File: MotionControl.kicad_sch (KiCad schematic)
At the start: 25 parts, among them J2 Conn_ARM_JTAG_SWD_10, Q1 2N7002, SW1 SW_Push, U1 ATSAMD21J18A-A, U7 TC4427, Y1 32.768kHz

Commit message: begin work on optical inputs, finish mag sensors
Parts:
- added J15: Conn_01x05_Pin, Connector_PinSocket_2.00mm:PinSocket_1x05_P2.00mm_Vertical, symbol Connector:Conn_01x05_Socket
- R8, R9: value 130R -> 165R; Part RC0402FR-07130RL -> RC0402FR-07165RL
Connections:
- net GND: now also J15.1 (Pin_1)
- net Mag Sensors/PWM1: now also J15.2 (Pin_2)
- net Mag Sensors/PWM2: now also J15.3 (Pin_3)
- net Mag Sensors/PWM3: now also J15.4 (Pin_4)
- net Mag Sensors/PWM4: now also J15.5 (Pin_5)
- net PB10_MAG_MOSI: now reaches U1.23 (PB10)
- net PB11_MAG_SCK: now reaches U1.24 (PB11)
- net PB12_MAG_CSn3: now reaches U1.25 (PB12)
- net PB13_MAG_CSn2: now reaches U1.26 (PB13)
- net PA18_MAG_CSn4: now reaches U1.37 (PA18)
- net PA22_MAG_MISO: now reaches U1.43 (PA22)
- net PA23_MAG_CSn1: now reaches U1.44 (PA23)
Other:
- added sheet Optical Sensors (opticalins.kicad_sch)

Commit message: cs routing changes, endstop stuff
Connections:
- net PA18_MAG_CSn4: now also U1.27 (PB14); no longer U1.37 (PA18)
- net PB07_ES5: now reaches U1.10 (PB07)
- net PB08_ES6: now reaches U1.11 (PB08)
- net PB06_ES7: now reaches U1.12 (PB09)
- net PB15_ES8: now reaches U1.28 (PB15)
- net PB16_ES9: now reaches U1.39 (PB16)
- net PB17_ES10: now reaches U1.40 (PB17)
- net PB22_ES11: now reaches U1.49 (PB22)
- net PB23_ES12: now reaches U1.50 (PB23)
- net PB30_MAG_CSn1: now reaches U1.59 (PB30)
- net PB05_ES3: now reaches U1.6 (PB05)
- net PB00_ES1: now reaches U1.61 (PB00)
- net PB01_ES2: now reaches U1.62 (PB01)
- net PB06_ES4: now reaches U1.9 (PB06)
- net PA23_MAG_CSn1: no longer names the net of U1.44 (PA23)

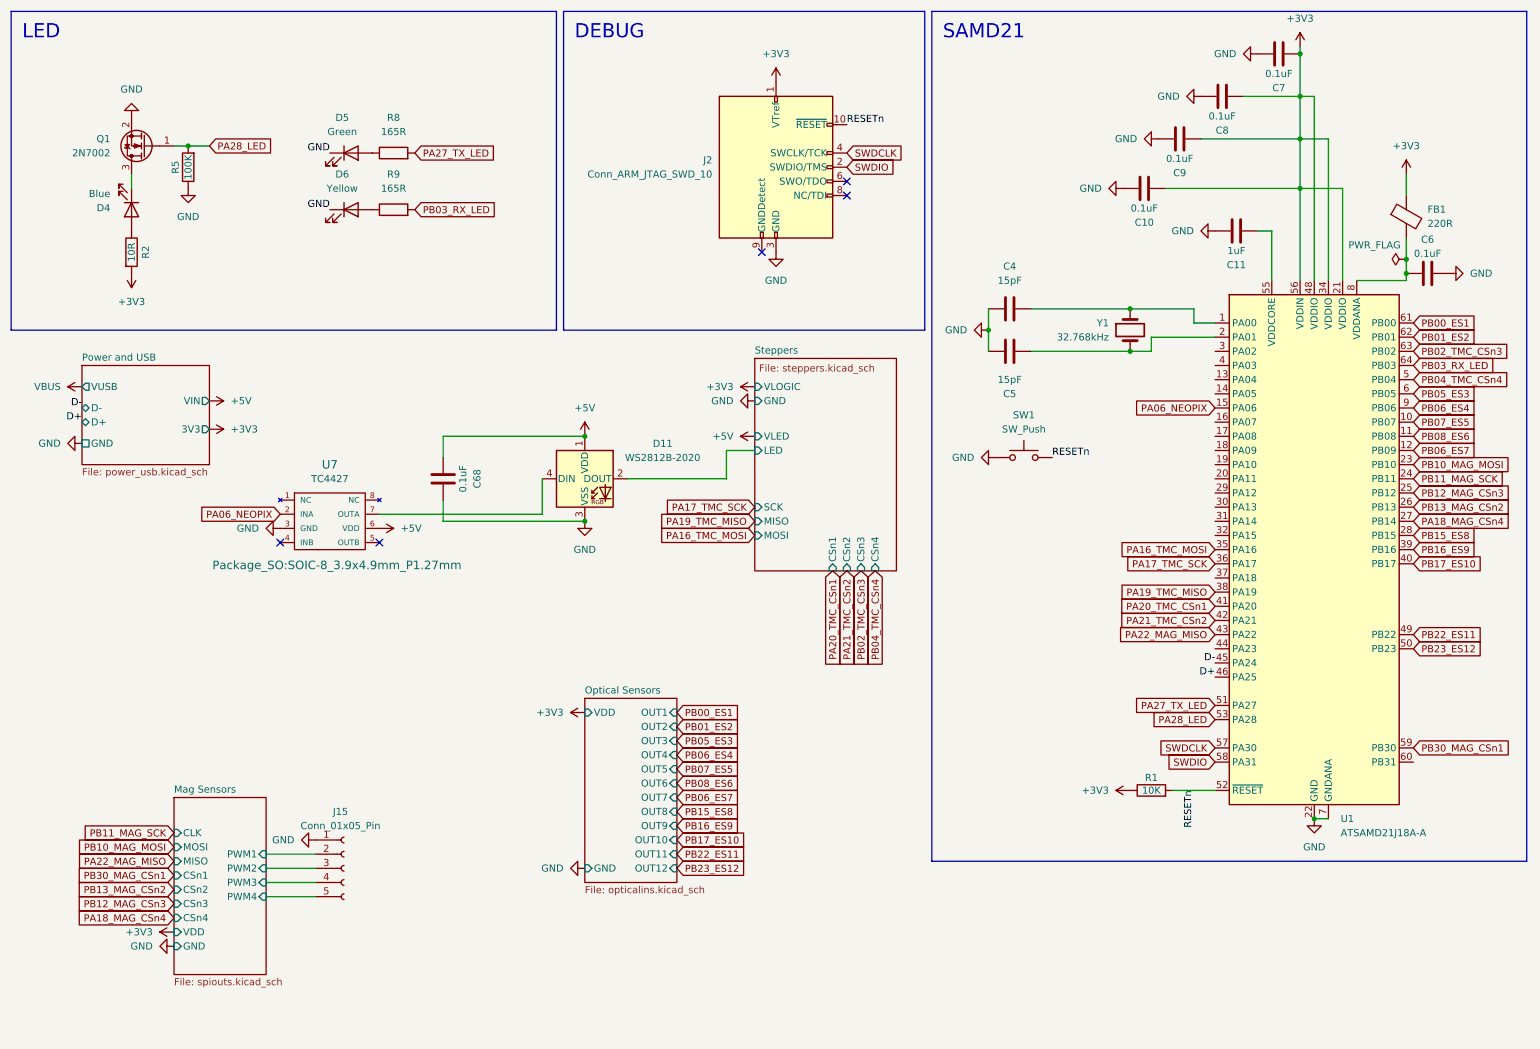
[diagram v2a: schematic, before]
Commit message: add spi master connector
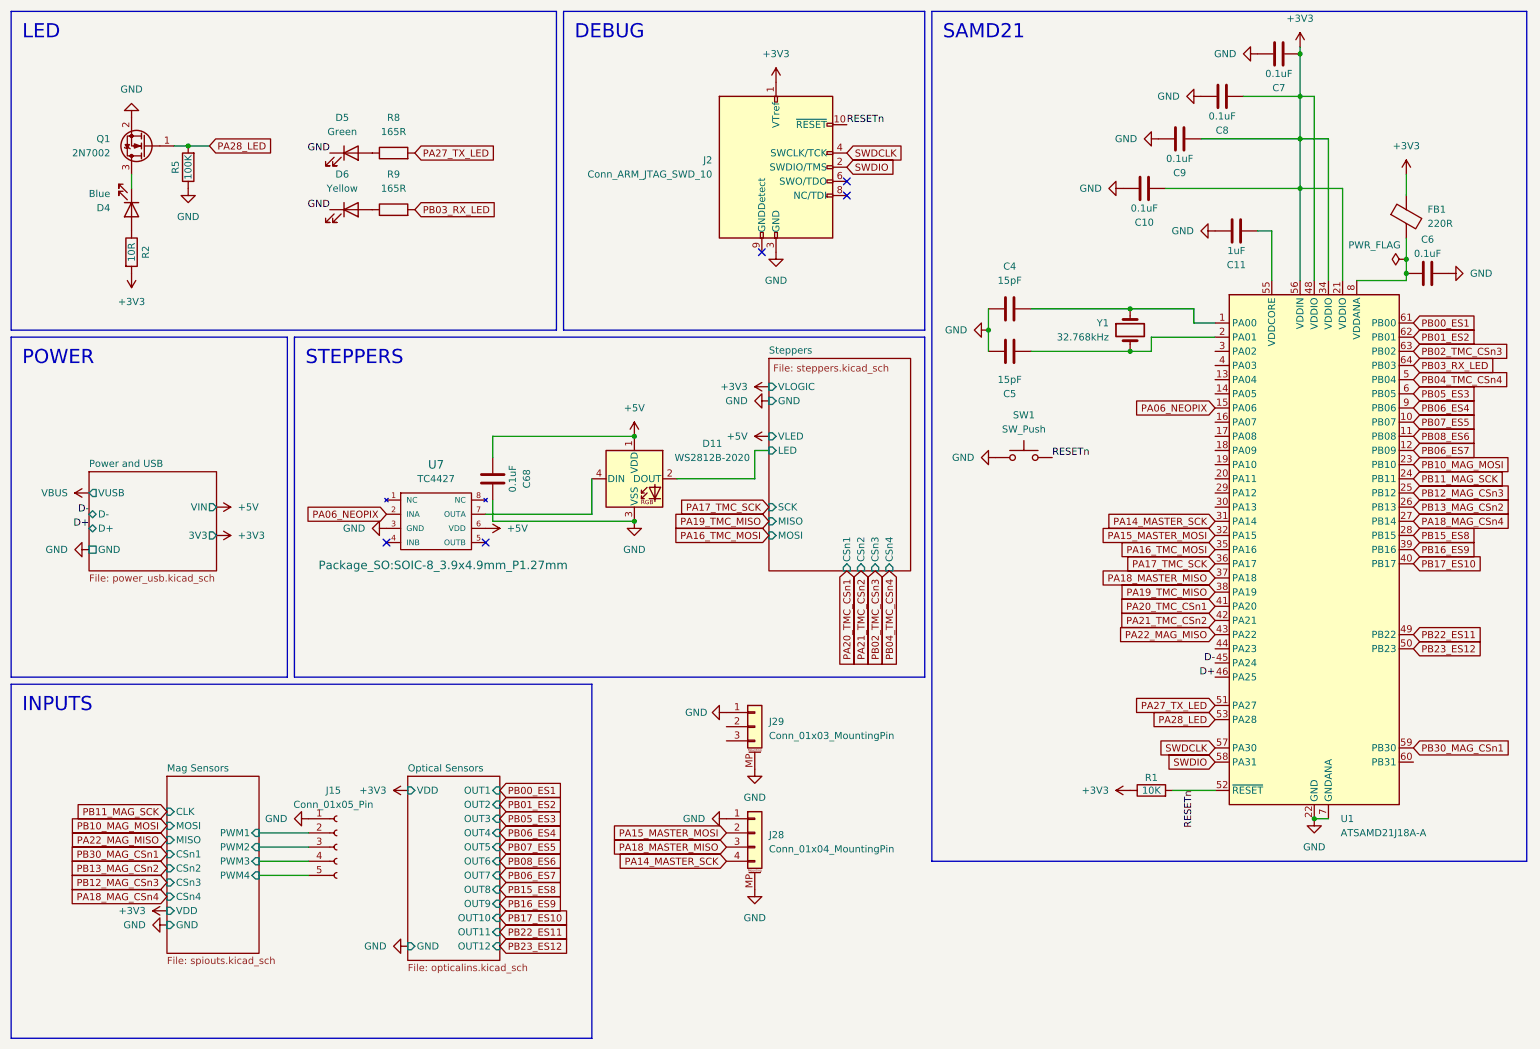
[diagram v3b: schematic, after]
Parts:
- added J28: Conn_01x04_MountingPin, Connector_JST:JST_SH_BM04B-SRSS-TB_1x04-1MP_P1.00mm_Vertical, symbol Connector_Generic_MountingPin:Conn_01x04_MountingPin
- added J29: Conn_01x03_MountingPin, Connector_JST:JST_SH_BM03B-SRSS-TB_1x03-1MP_P1.00mm_Vertical, symbol Connector_Generic_MountingPin:Conn_01x03_MountingPin
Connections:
- net GND: now also J28.1 (Pin_1), J28.MP (MountPin), J29.1 (Pin_1), J29.MP (MountPin)
- net PA14_MASTER_SCK: now reaches U1.31 (PA14)
- net PA14_MASTER_SCK: now also J28.4 (Pin_4)
- net PA15_MASTER_MOSI: now reaches U1.32 (PA15)
- net PA15_MASTER_MOSI: now also J28.2 (Pin_2)
- net PA18_MASTER_MISO: now reaches U1.37 (PA18)
- net PA18_MASTER_MISO: now also J28.3 (Pin_3)
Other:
- moved on the sheet: C68, D11, J15, U7

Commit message: add spi cs pin, remove center endstop support
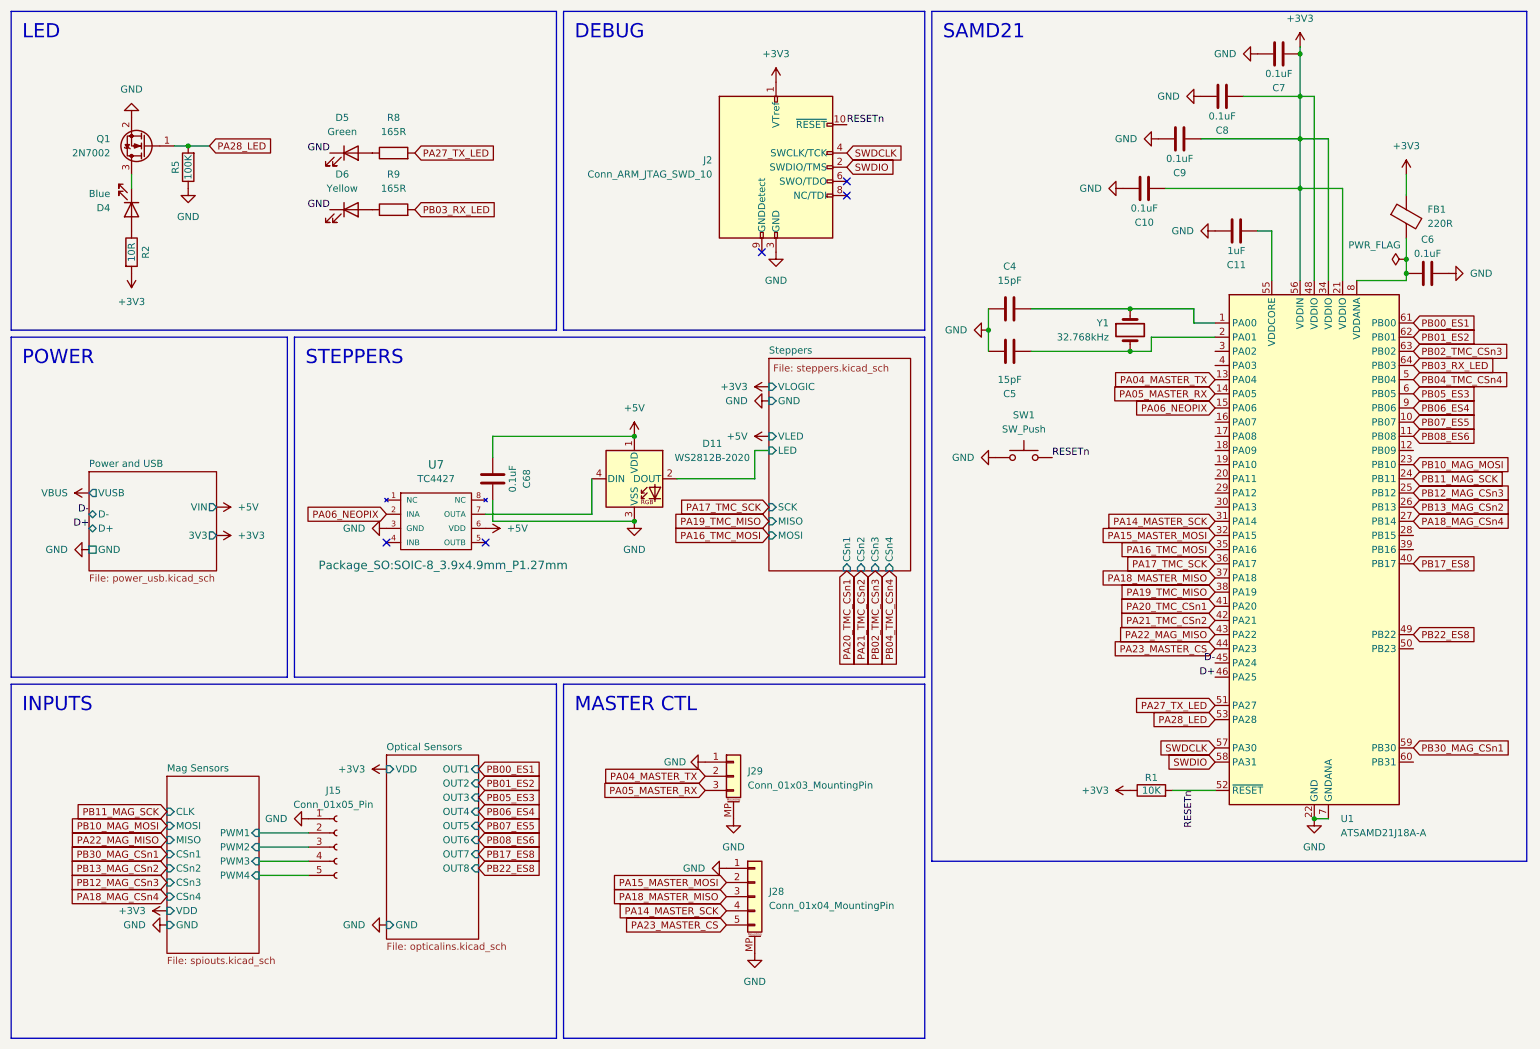
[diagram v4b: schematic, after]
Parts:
- J28: footprint Connector_JST:JST_SH_BM04B-SRSS-TB_1x04-1MP_P1.00mm_Vertical -> Connector_JST:JST_SH_BM05B-SRSS-TB_1x05-1MP_P1.00mm_Vertical; symbol Connector_Generic_MountingPin:Conn_01x04_MountingPin -> Connector_Generic_MountingPin:Conn_01x05_MountingPin
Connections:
- net PA04_MASTER_TX: now reaches U1.13 (PA04)
- net PA04_MASTER_TX: now also J29.2 (Pin_2)
- net PA05_MASTER_RX: now reaches U1.14 (PA05)
- net PA05_MASTER_RX: now also J29.3 (Pin_3)
- net PA23_MASTER_CS: now reaches U1.44 (PA23)
- net PA23_MASTER_CS: now also J28.5 (Pin_5)
- net PB06_ES7: no longer names the net of U1.12 (PB09)
- net PB15_ES8: no longer names the net of U1.28 (PB15)
- net PB16_ES9: no longer names the net of U1.39 (PB16)
- net PB17_ES10 renamed PB17_ES8
- net PB22_ES11 renamed PB22_ES8
- net PB23_ES12: no longer names the net of U1.50 (PB23)
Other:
- sheet Optical Sensors ports: added none; removed OUT10, OUT11, OUT12, OUT9
- moved on the sheet: J29
